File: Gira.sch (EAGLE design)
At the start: 24 parts, among them IC1 MEGA8-PTQFP, Q2 2N7002

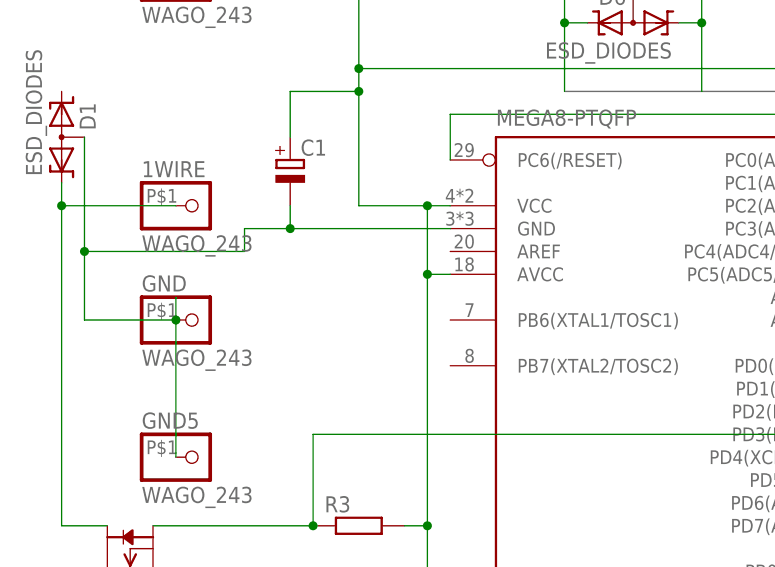
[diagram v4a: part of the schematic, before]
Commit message: V 2.2
added Aref capacitor
fixed power supply via prog connector problem
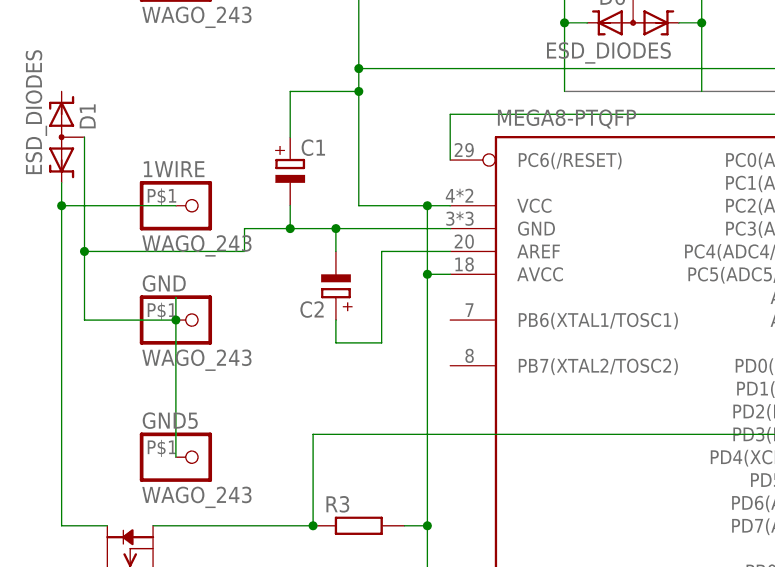
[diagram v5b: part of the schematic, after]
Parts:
- added C2: (no value), common:CP1206
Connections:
- removed net 5V: U$1.2
- new net N$1: C2.+, IC1.AREF
- net 3V3: now also U$1.2
- net GND: now also C2.-
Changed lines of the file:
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@@
 </variantdefs>
 <classes>
-<class number="0" name="default" width="0" drill="0">
+<class number="0" name="default" width="0.35" drill="0">
 </class>
 <class number="1" name="power" width="1" drill="0">
@@
 <part name="Q2" library="common" deviceset="2N7002" device=""/>
 <part name="R3" library="common" deviceset="R-EU_" device="R0603"/>
+<part name="C2" library="common" deviceset="CP" device="1206"/>
 </parts>
 <sheets>
@@
 <instance part="Q2" gate="&gt;NAME" x="-2.54" y="22.86" rot="R90"/>
 <instance part="R3" gate="G$1" x="22.86" y="30.48"/>
+<instance part="C2" gate="G$1" x="20.32" y="55.88" rot="R180"/>
 </instances>
 <busses>
@@
 <wire x1="99.06" y1="58.42" x2="106.68" y2="58.42" width="0.1524" layer="91"/>
 <junction x="99.06" y="58.42"/>
-</segment>
-</net>
-<net name="5V" class="1">
-<segment>
-<pinref part="P+1" gate="VCC" pin="VCC"/>
-<wire x1="33.02" y1="5.08" x2="40.64" y2="5.08" width="0.1524" layer="91"/>
-<wire x1="40.64" y1="5.08" x2="40.64" y2="-5.08" width="0.1524" layer="91"/>
-<pinref part="U$1" gate="G$1" pin="2"/>
-<wire x1="40.64" y1="-5.08" x2="48.26" y2="-5.08" width="0.1524" layer="91"/>
 </segment>
 </net>
@@
 <junction x="2.54" y="53.34"/>
 <pinref part="IC1" gate="G$1" pin="GND"/>
-<wire x1="33.02" y1="63.5" x2="15.24" y2="63.5" width="0.1524" layer="91"/>
+<wire x1="33.02" y1="63.5" x2="20.32" y2="63.5" width="0.1524" layer="91"/>
+<wire x1="20.32" y1="63.5" x2="15.24" y2="63.5" width="0.1524" layer="91"/>
 <wire x1="15.24" y1="63.5" x2="10.16" y2="63.5" width="0.1524" layer="91"/>
 <wire x1="10.16" y1="63.5" x2="10.16" y2="60.96" width="0.1524" layer="91"/>
@@
 <pinref part="GND5" gate="G$1" pin="1"/>
 <wire x1="2.54" y1="38.1" x2="2.54" y2="53.34" width="0.1524" layer="91"/>
+<pinref part="C2" gate="G$1" pin="-"/>
+<wire x1="20.32" y1="60.96" x2="20.32" y2="63.5" width="0.1524" layer="91"/>
+<junction x="20.32" y="63.5"/>
 </segment>
 <segment>
@@
 <junction x="30.48" y="30.48"/>
 </segment>
+<segment>
+<pinref part="P+1" gate="VCC" pin="VCC"/>
+<wire x1="33.02" y1="5.08" x2="40.64" y2="5.08" width="0.1524" layer="91"/>
+<wire x1="40.64" y1="5.08" x2="40.64" y2="-5.08" width="0.1524" layer="91"/>
+<pinref part="U$1" gate="G$1" pin="2"/>
+<wire x1="40.64" y1="-5.08" x2="48.26" y2="-5.08" width="0.1524" layer="91"/>
+</segment>
 </net>
 <net name="N$3" class="0">
@@
 </segment>
 </net>
+<net name="N$1" class="0">
+<segment>
+<pinref part="IC1" gate="G$1" pin="AREF"/>
+<wire x1="33.02" y1="60.96" x2="25.4" y2="60.96" width="0.1524" layer="91"/>
+<wire x1="25.4" y1="60.96" x2="25.4" y2="50.8" width="0.1524" layer="91"/>
+<pinref part="C2" gate="G$1" pin="+"/>
+<wire x1="25.4" y1="50.8" x2="20.32" y2="50.8" width="0.1524" layer="91"/>
+<wire x1="20.32" y1="50.8" x2="20.32" y2="53.34" width="0.1524" layer="91"/>
+</segment>
+</net>

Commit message: V2.2
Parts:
- removed D3: ESD_DIODES, common:ESD_DIODES
- removed GND: WAGO_243, common:WAGO_243
- added D7: ESD_DIODES, common:ESD_DIODES
- added Q1, Q3: 2N7002, common:2N7002
- added R1, R2: (no value), common:R-EU_R0603
- added _SCL2, _SDA2: WAGO_243, common:WAGO_243
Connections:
- new net N$4: D7.K1, Q3.D, _SDA2.1
- new net N$5: D7.K2, Q1.D, _SCL2.1
- new net SCL2: IC1.PC5(ADC5/SCL), Q1.S, R2.1
- new net SDA2: IC1.PC4(ADC4/SDA), Q3.S, R1.1
- new net VCC: Q1.G, Q3.G, R1.2, R2.2
- net GND: now also D7.AA; no longer D3.AA, GND.1
- net N$16: now also D1.K1, IC1.PD3(INT1); no longer D3.K1, IC1.PD2(INT0)
- net N$2: now also IC1.PD2(INT0); no longer IC1.PD3(INT1)
- net N$3: now also D1.K2; no longer D1.K1
- net SCL: now also IC1.ADC7; no longer IC1.PC5(ADC5/SCL)
- net SDA: now also IC1.ADC6; no longer IC1.PC4(ADC4/SDA)
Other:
- moved on the sheet: D1
